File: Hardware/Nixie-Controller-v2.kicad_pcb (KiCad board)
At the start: 4 copper layers, 220 x 65 mm, 227 parts, among them J7 12V DC JACK, J8 RST, U1 MAX1771, U10 74HC4067, U11 M41T01, U12 STM32F103C8, U13 OPA180, U14 74HC4067, U15 OPA180, U16 74HC4067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

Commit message: Update testpoints & decrease size
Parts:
- removed TP17: TX, TestPoint:TestPoint_Pad_D2.5mm
- added TP19: ~, TestPoint:TestPoint_Pad_D1.5mm, B.Cu at (99.8, 60.0)
- added TPr: TX, TestPoint:TestPoint_Pad_D1.5mm, B.Cu at (94.7, 60.0)
- TP1, TP11, TP14, TP15, TP16, TP18, TP2, TP7: footprint TestPoint:TestPoint_Pad_D2.5mm -> TestPoint:TestPoint_Pad_D1.5mm
- moved TP18 1.74 mm to (97.3, 60.0)
- moved TP15 0.25 mm to (123.0, 83.0), turned to 0 degrees
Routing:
- net GND: track 68.3 -> 69.7 mm, vias 379 -> 380

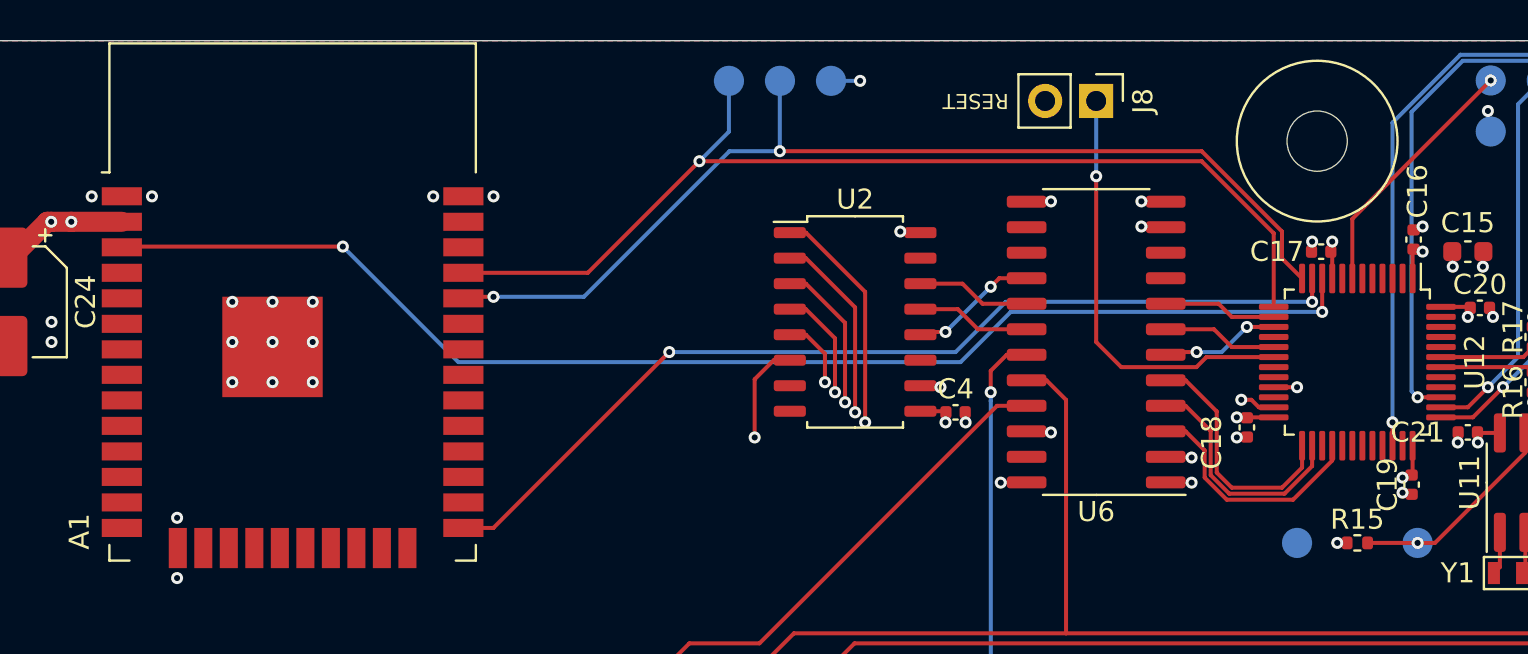
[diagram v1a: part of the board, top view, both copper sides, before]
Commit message: Use correct UART ports for ESP32-WROOM-32
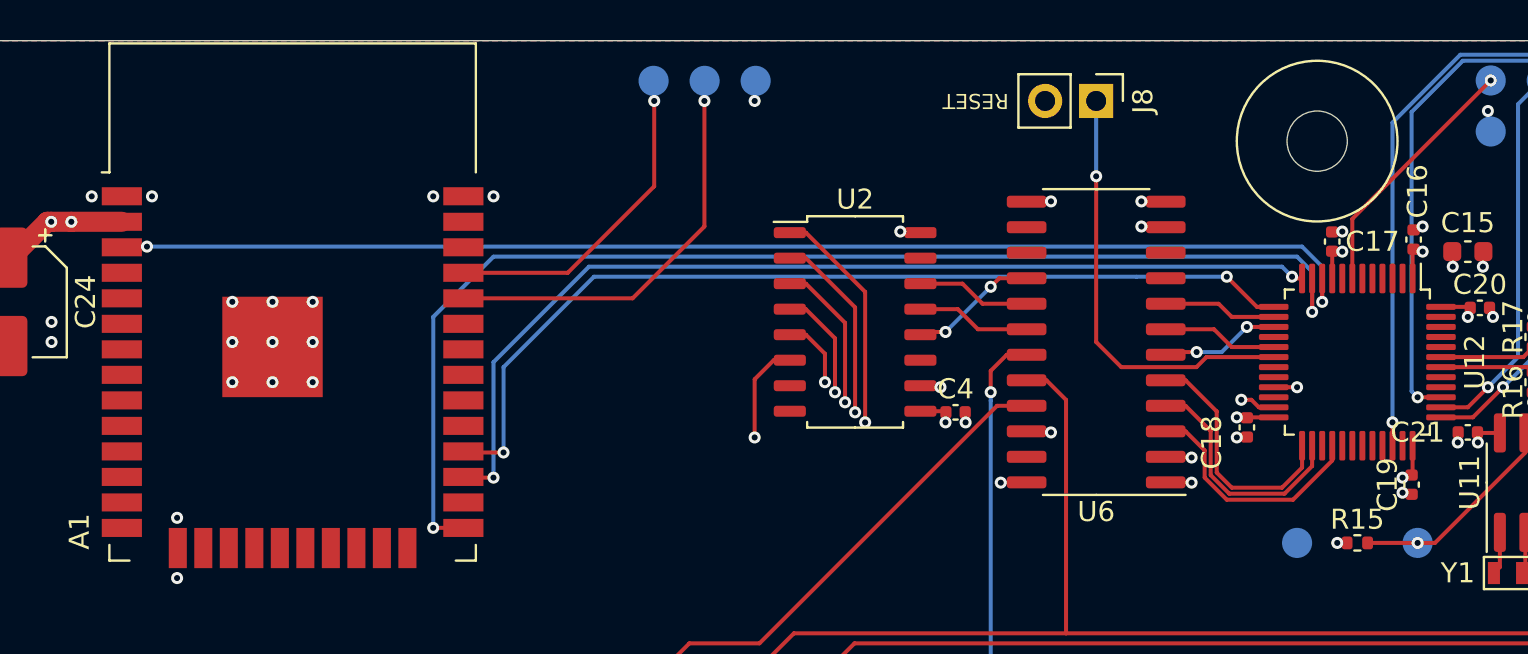
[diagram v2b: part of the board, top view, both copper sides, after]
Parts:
- moved TP17 3.75 mm to (91.0, 60.0)
- moved TP18 3.75 mm to (93.5, 60.0)
- moved TP19 3.75 mm to (96.0, 60.0)
- moved C17 0.74 mm to (124.8, 68.0), turned to 90 degrees
- renumbered TPr to TP17
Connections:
- A1 pad 27: Net-(A1-Pad27) -> ESP_TX
- A1 pad 28: Net-(A1-Pad28) -> ESP_RX
- A1 pad 34: ESP_TX -> ESP_LOG_RX
- A1 pad 35: ESP_RX -> ESP_LOG_TX
- TP17 pad 1: ESP_RX -> ESP_LOG_TX
- TP18 pad 1: ESP_TX -> ESP_LOG_RX
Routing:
- net ESP_LOG_RX: track 0.00 -> 20.7 mm, vias 0 -> 1
- net ESP_LOG_TX: track 0.00 -> 16.5 mm, vias 0 -> 1
- net ESP_RUN: track 48.1 -> 61.0 mm
- net ESP_RX: track 52.4 -> 47.1 mm, vias 1 -> 2
- net ESP_TX: track 51.7 -> 49.7 mm
- net ESP_nRST: track 64.8 -> 63.1 mm

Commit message: Change silkscreen text for v2.0-pre3
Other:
- board text added: "Revision: v2.0-pre3"
- board text removed: "Revision: v2.0-pre2"
